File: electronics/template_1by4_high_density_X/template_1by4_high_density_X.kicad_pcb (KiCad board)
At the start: 2 copper layers, 19 x 34 mm, 12 parts, among them J1 1, J10 10, J2 2, J3 3, J4 4, J5 5, J6 6, J7 7, J8 8, J9 9

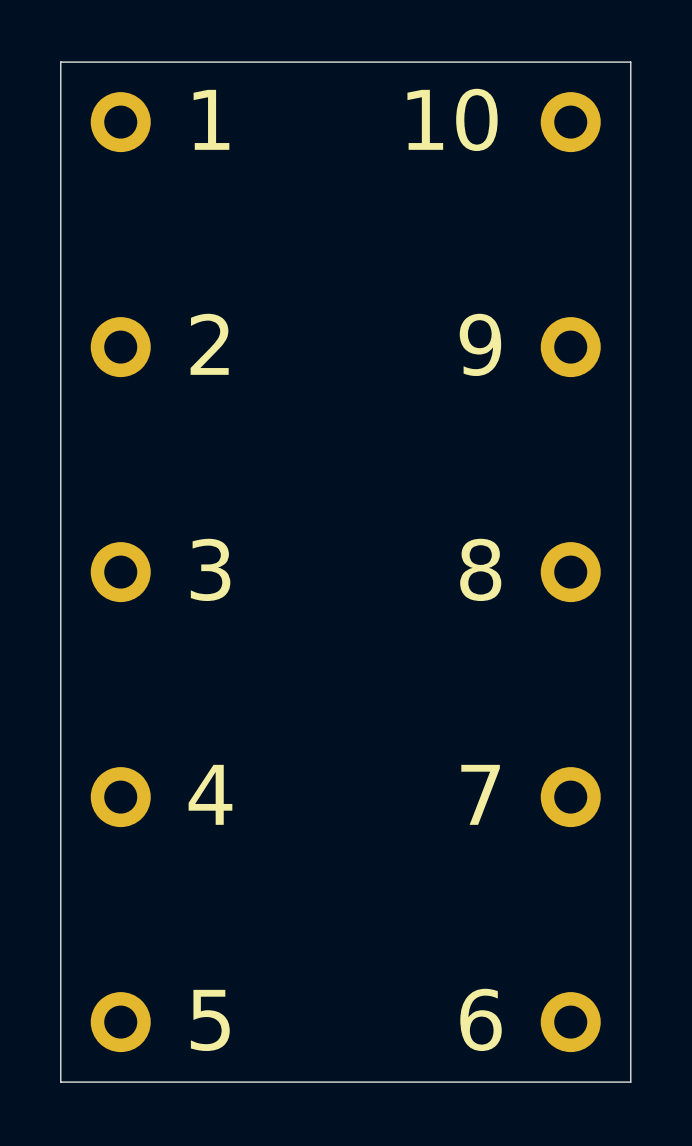
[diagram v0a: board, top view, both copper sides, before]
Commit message: completed high density X templates, updated versionnumbers of high density XN templates
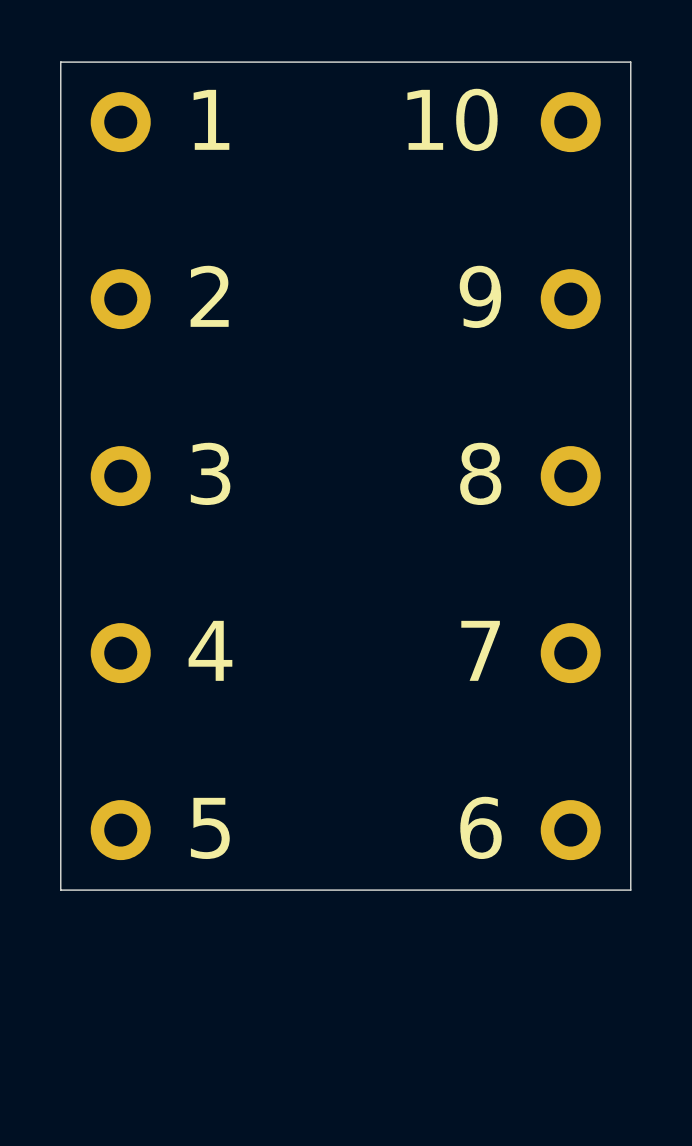
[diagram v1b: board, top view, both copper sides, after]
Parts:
- moved J5 6.40 mm to (142.5, 86.1)
- moved J6 6.40 mm to (157.5, 86.1)
- moved J4 4.80 mm to (142.5, 80.2)
- moved J7 4.80 mm to (157.5, 80.2)
- moved J3 3.20 mm to (142.5, 74.3)
- moved J8 3.20 mm to (157.5, 74.3)
- moved N1 3.00 mm to (150.9, 77.2)
- moved N2 3.00 mm to (150.0, 73.5)
- moved J2 1.60 mm to (142.5, 68.4)
- moved J9 1.60 mm to (157.5, 68.4)
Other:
- board size 19 x 34 mm -> 19 x 27.6 mm
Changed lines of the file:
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@@
   )
   (footprint "mill-max:PC_pin_nail_head_6092" locked (layer "F.Cu")
-    (at 142.5 70)
+    (at 142.5 68.4)
     (property "Sheetfile" "template_1by4.kicad_sch")
     (property "Sheetname" "")
@@
   )
   (footprint "mill-max:PC_pin_nail_head_6092" locked (layer "F.Cu")
-    (at 142.5 77.5)
+    (at 142.5 74.3)
     (property "Sheetfile" "template_1by4.kicad_sch")
     (property "Sheetname" "")
@@
   )
   (footprint "mill-max:PC_pin_nail_head_6092" locked (layer "F.Cu")
-    (at 142.5 92.5 180)
+    (at 142.5 86.1 180)
     (property "Sheetfile" "template_1by4.kicad_sch")
     (property "Sheetname" "")
@@
   )
   (footprint "mill-max:PC_pin_nail_head_6092" locked (layer "F.Cu")
-    (at 157.5 92.5)
+    (at 157.5 86.1)
     (property "Sheetfile" "template_1by4.kicad_sch")
     (property "Sheetname" "")
@@
   )
   (footprint "mill-max:PC_pin_nail_head_6092" locked (layer "F.Cu")
-    (at 142.5 85 180)
+    (at 142.5 80.2 180)
     (property "Sheetfile" "template_1by4.kicad_sch")
     (property "Sheetname" "")
@@
   )
   (footprint "mill-max:PC_pin_nail_head_6092" locked (layer "F.Cu")
-    (at 157.5 77.5)
+    (at 157.5 74.3)
     (property "Sheetfile" "template_1by4.kicad_sch")
     (property "Sheetname" "")
@@
   )
   (footprint "mill-max:PC_pin_nail_head_6092" locked (layer "F.Cu")
-    (at 157.5 85)
+    (at 157.5 80.2)
     (property "Sheetfile" "template_1by4.kicad_sch")
     (property "Sheetname" "")
@@
   )
   (footprint "mill-max:PC_pin_nail_head_6092" locked (layer "F.Cu")
-    (at 157.5 70)
+    (at 157.5 68.4)
     (property "Sheetfile" "template_1by4.kicad_sch")
     (property "Sheetname" "")
@@
   )
   (footprint "Symbol:OSHW-Symbol_6.7x6mm_SilkScreen" (layer "B.Cu")
-    (at 150 76.5 180)
+    (at 150 73.5 180)
     (descr "Open Source Hardware Symbol")
     (tags "Logo Symbol OSHW")
@@
   )
   (footprint "SquantorLabels:Label_Generic" (layer "B.Cu")
-    (at 150.9 80.2 180)
+    (at 150.9 77.2 180)
     (descr "Label for general purpose use")
     (tags "Label")
@@
       (stroke (width 0.15) (type solid)) (layer "B.SilkS"))
   )
-  (gr_line (start 140.5 94.5) (end 159.5 94.5)
+  (gr_line (start 140.5 88.1) (end 159.5 88.1)
     (stroke (width 0.05) (type solid)) (layer "Edge.Cuts"))
-  (gr_line (start 159.5 60.5) (end 159.5 94.5)
+  (gr_line (start 159.5 60.5) (end 159.5 88.1)
     (stroke (width 0.05) (type solid)) (layer "Edge.Cuts"))
   (gr_line (start 159.5 60.5) (end 140.5 60.5)
     (stroke (width 0.05) (type solid)) (layer "Edge.Cuts"))
-  (gr_line (start 140.5 94.5) (end 140.5 60.5)
+  (gr_line (start 140.5 88.1) (end 140.5 60.5)
     (stroke (width 0.05) (type solid)) (layer "Edge.Cuts"))
 )
